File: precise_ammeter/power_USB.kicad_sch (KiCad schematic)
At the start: 0 parts

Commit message: Dodano Sekcje zasilanie MCU i wzmacniaczy oraz konektor USB
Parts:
- added C1, C22, C23, C25, C26, C5: 2u2, Capacitor_SMD:C_0805_2012Metric_Pad1.18x1.45mm_HandSolder, symbol Device:C
- added C24, C27: 10u, Capacitor_SMD:CP_Elec_4x5.4, symbol Device:C_Polarized
- added C28: 1n, Capacitor_SMD:C_0805_2012Metric_Pad1.18x1.45mm_HandSolder, symbol Device:C_Small
- added D1, D2: Green, LED_SMD:LED_0805_2012Metric_Pad1.15x1.40mm_HandSolder, symbol Device:LED
- added J3: USB4110GFA, USB4100GFA:GCT_USB4110GFA, symbol USB4110GFA:USB4110GFA
- added U10, U8: TPS7A2450DBVR, TPS7A2450DBVR:SOT_50DBVR, symbol TPS7A2450DBVR:TPS7A2450DBVR
- added U7: TPS7A2433DBVR, SOT23_DBV_TEX, symbol TPS7A2433DBVR:TPS7A2433DBVR
- added U9: LMC7660, Package_SO:SOIC-8_3.9x4.9mm_P1.27mm, symbol Regulator_SwitchedCapacitor:LMC7660
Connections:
- new net: C28.2, U9.7 (OSC)
- new net: C24.1, U9.2 (CAP+)
- new net: C24.2, U9.4 (CAP-)
- new net +3V3: C5.1, D2.2 (A), U7.5 (Vout)
- new net +5VA: C23.1, D1.2 (A), U8.5 (Vout)
- new net +5V_U9: C26.1, C28.1, U10.5 (Vout), U9.8 (V+)
- new net -5VA: C27.2, U9.5 (VOUT)
- new net GND: C1.2, C22.2, C23.2, C25.2, C26.2, C27.1, C5.2, D1.1 (K), D2.1 (K), J3.A1/B12 (GND), J3.B1/A12 (GND), J3.S1 (GND), J3.S2 (GND), J3.S3 (GND), J3.S4 (GND), U10.2 (GND), U7.2 (GND), U8.2 (GND), U9.3 (GND)
- new net USB_D_N: J3.A7 (DN1), J3.B7 (DN2)
- new net USB_D_P: J3.A6 (DP1), J3.B6 (DP2)
- new net VBUS: C1.1, C22.1, C25.1, U10.1 (Vin), U10.3 (EN), U7.1 (Vin), U7.3 (EN), U8.1 (Vin), U8.3 (EN)
- no-connect marks 0 -> 10
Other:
- note added: "+3V3 STM32 power supply"
- note added: "+5VA for analog section"
- note added: "-5VA for analog section"
- note added: "Power status LEDs"
- note added: "USB 2.0 Type C for data transfer only"

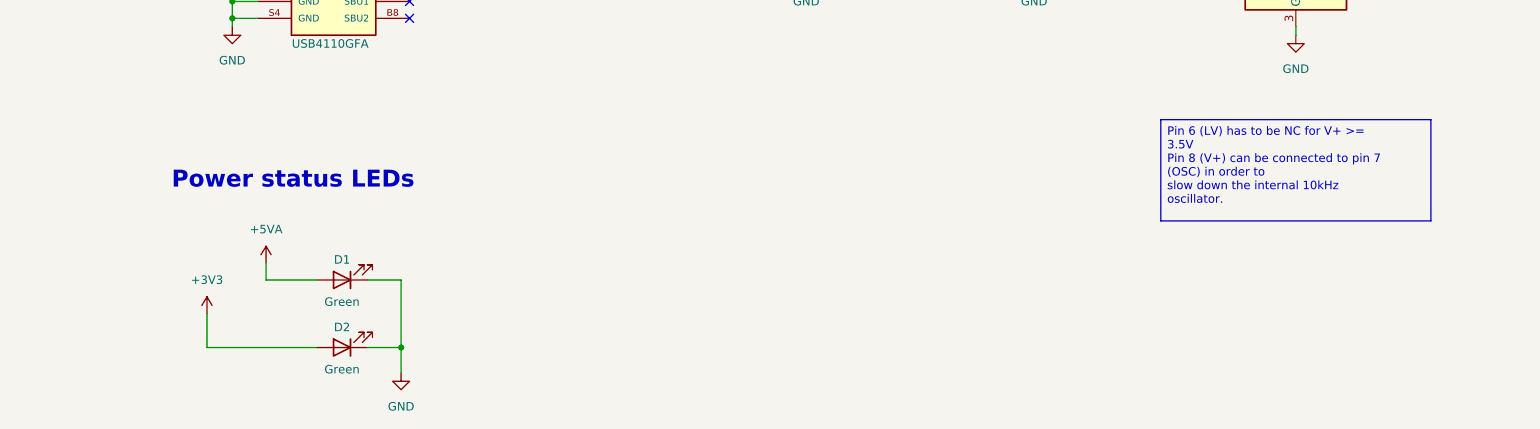
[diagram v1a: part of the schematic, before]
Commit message: dodano rezystory do diod LED
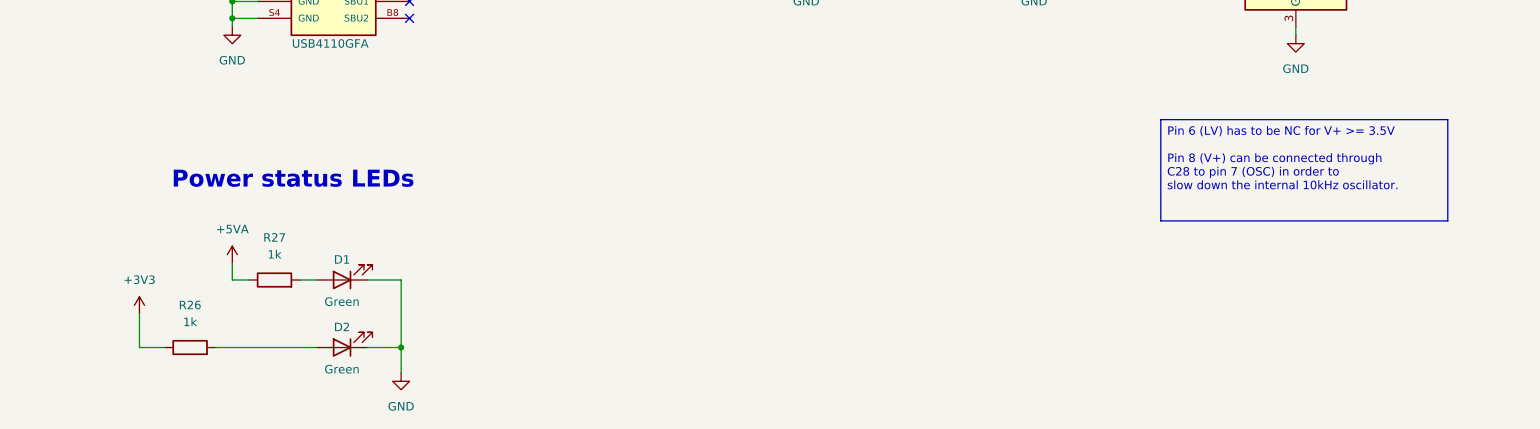
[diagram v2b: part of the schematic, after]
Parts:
- added R26, R27: 1k, Resistor_SMD:R_0805_2012Metric_Pad1.20x1.40mm_HandSolder, symbol Device:R
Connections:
- net +3V3: now also R26.1; no longer D2.2 (A)
- net +5VA: now also R27.1; no longer D1.2 (A)
- new net: D1.2 (A), R27.2
- new net: D2.2 (A), R26.2
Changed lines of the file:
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@@
 		)
 	)
-	(text_box "Pin 6 (LV) has to be NC for V+ >= 3.5V\nPin 8 (V+) can be connected to pin 7 (OSC) in order to\nslow down the internal 10kHz oscillator."
+	(text_box "Pin 6 (LV) has to be NC for V+ >= 3.5V\n\nPin 8 (V+) can be connected through C28 to pin 7 (OSC) in order to\nslow down the internal 10kHz oscillator."
 		(exclude_from_sim no)
 		(at 220.98 144.78 0)
-		(size 40.64 15.24)
+		(size 43.18 15.24)
 		(margins 0.9525 0.9525 0.9525 0.9525)
 		(stroke
@@
 	(wire
 		(pts
+			(xy 81.28 168.91) (xy 83.82 168.91)
+		)
+		(stroke
+			(width 0)
+			(type default)
+		)
+	)
+	(wire
+		(pts
 			(xy 198.12 45.72) (xy 198.12 44.45)
 		)
@@
 	(wire
 		(pts
-			(xy 93.98 179.07) (xy 77.47 179.07)
+			(xy 81.28 114.3) (xy 81.28 116.84)
 		)
 		(stroke
@@
 	(wire
 		(pts
-			(xy 81.28 114.3) (xy 81.28 116.84)
+			(xy 106.68 57.15) (xy 106.68 55.88)
 		)
 		(stroke
@@
 	(wire
 		(pts
-			(xy 106.68 57.15) (xy 106.68 55.88)
+			(xy 232.41 55.88) (xy 232.41 54.61)
 		)
 		(stroke
@@
 	(wire
 		(pts
-			(xy 232.41 55.88) (xy 232.41 54.61)
+			(xy 110.49 121.92) (xy 118.11 121.92)
 		)
 		(stroke
@@
 	(wire
 		(pts
-			(xy 110.49 121.92) (xy 118.11 121.92)
+			(xy 67.31 179.07) (xy 71.12 179.07)
 		)
 		(stroke
@@
 	(wire
 		(pts
+			(xy 78.74 179.07) (xy 93.98 179.07)
+		)
+		(stroke
+			(width 0)
+			(type default)
+		)
+	)
+	(wire
+		(pts
 			(xy 81.28 116.84) (xy 85.09 116.84)
 		)
@@
 	(wire
 		(pts
-			(xy 86.36 166.37) (xy 86.36 168.91)
+			(xy 81.28 166.37) (xy 81.28 168.91)
 		)
 		(stroke
@@
 	(wire
 		(pts
-			(xy 77.47 179.07) (xy 77.47 173.99)
+			(xy 67.31 179.07) (xy 67.31 173.99)
 		)
 		(stroke
@@
 	(wire
 		(pts
-			(xy 93.98 168.91) (xy 86.36 168.91)
-		)
-		(stroke
-			(width 0)
-			(type default)
-		)
-	)
-	(wire
-		(pts
 			(xy 81.28 124.46) (xy 85.09 124.46)
 		)
@@
 	(wire
 		(pts
+			(xy 91.44 168.91) (xy 93.98 168.91)
+		)
+		(stroke
+			(width 0)
+			(type default)
+		)
+	)
+	(wire
+		(pts
 			(xy 273.05 106.68) (xy 273.05 110.49)
 		)
@@
 	)
 	(symbol
+		(lib_id "Device:R")
+		(at 87.63 168.91 90)
+		(unit 1)
+		(exclude_from_sim no)
+		(in_bom yes)
+		(on_board yes)
+		(dnp no)
+		(fields_autoplaced yes)
+		(property "Reference" "R27"
+			(at 87.63 162.56 90)
+			(effects
+				(font
+					(size 1.27 1.27)
+				)
+			)
+		)
+		(property "Value" "1k"
+			(at 87.63 165.1 90)
+			(effects
+				(font
+					(size 1.27 1.27)
+				)
+			)
+		)
+		(property "Footprint" "Resistor_SMD:R_0805_2012Metric_Pad1.20x1.40mm_HandSolder"
+			(at 87.63 170.688 90)
+			(effects
+				(font
+					(size 1.27 1.27)
+				)
+				(hide yes)
+			)
+		)
+		(property "Datasheet" "~"
+			(at 87.63 168.91 0)
+			(effects
+				(font
+					(size 1.27 1.27)
+				)
+				(hide yes)
+			)
+		)
+		(property "Description" "Resistor"
+			(at 87.63 168.91 0)
+			(effects
+				(font
+					(size 1.27 1.27)
+				)
+				(hide yes)
+			)
+		)
+		(pin "2"
+		)
+		(pin "1"
+		)
+		(instances
+			(project ""
+				(path "/7da3b652-85ac-4caa-8d8d-9cad461e9c85/9e6d6147-95e6-4ef0-a238-5628802dd2a2"
+					(reference "R27")
+					(unit 1)
+				)
+			)
+		)
+	)
+	(symbol
 		(lib_id "Device:C_Small")
 		(at 224.79 114.3 0)
@@
 	(symbol
 		(lib_id "power:+5VA")
-		(at 86.36 166.37 0)
+		(at 81.28 166.37 0)
 		(unit 1)
 		(exclude_from_sim no)
@@
 		(fields_autoplaced yes)
 		(property "Reference" "#PWR062"
-			(at 86.36 170.18 0)
+			(at 81.28 170.18 0)
 			(effects
 				(font
@@
 		)
 		(property "Value" "+5VA"
-			(at 86.36 161.29 0)
+			(at 81.28 161.29 0)
 			(effects
 				(font
@@
 		)
 		(property "Footprint" ""
-			(at 86.36 166.37 0)
+			(at 81.28 166.37 0)
 			(effects
 				(font
@@
 		)
 		(property "Datasheet" ""
-			(at 86.36 166.37 0)
+			(at 81.28 166.37 0)
 			(effects
 				(font
@@
 		)
 		(property "Description" "Power symbol creates a global label with name \"+5VA\""
-			(at 86.36 166.37 0)
+			(at 81.28 166.37 0)
 			(effects
 				(font
@@
 	)
 	(symbol
+		(lib_id "Device:R")
+		(at 74.93 179.07 90)
+		(unit 1)
+		(exclude_from_sim no)
+		(in_bom yes)
+		(on_board yes)
+		(dnp no)
+		(fields_autoplaced yes)
+		(property "Reference" "R26"
+			(at 74.93 172.72 90)
+			(effects
+				(font
+					(size 1.27 1.27)
+				)
+			)
+		)
+		(property "Value" "1k"
+			(at 74.93 175.26 90)
+			(effects
+				(font
+					(size 1.27 1.27)
+				)
+			)
+		)
+		(property "Footprint" "Resistor_SMD:R_0805_2012Metric_Pad1.20x1.40mm_HandSolder"
+			(at 74.93 180.848 90)
+			(effects
+				(font
+					(size 1.27 1.27)
+				)
+				(hide yes)
+			)
+		)
+		(property "Datasheet" "~"
+			(at 74.93 179.07 0)
+			(effects
+				(font
+					(size 1.27 1.27)
+				)
+				(hide yes)
+			)
+		)
+		(property "Description" "Resistor"
+			(at 74.93 179.07 0)
+			(effects
+				(font
+					(size 1.27 1.27)
+				)
+				(hide yes)
+			)
+		)
+		(pin "2"
+		)
+		(pin "1"
+		)
+		(instances
+			(project ""
+				(path "/7da3b652-85ac-4caa-8d8d-9cad461e9c85/9e6d6147-95e6-4ef0-a238-5628802dd2a2"
+					(reference "R26")
+					(unit 1)
+				)
+			)
+		)
+	)
+	(symbol
 		(lib_id "power:GND")
 		(at 72.39 57.15 0)
@@
 	(symbol
 		(lib_id "power:+3V3")
-		(at 77.47 173.99 0)
+		(at 67.31 173.99 0)
 		(unit 1)
 		(exclude_from_sim no)
@@
 		(fields_autoplaced yes)
 		(property "Reference" "#PWR063"
-			(at 77.47 177.8 0)
+			(at 67.31 177.8 0)
 			(effects
 				(font
@@
 		)
 		(property "Value" "+3V3"
-			(at 77.47 168.91 0)
+			(at 67.31 168.91 0)
 			(effects
 				(font
@@
 		)
 		(property "Footprint" ""
-			(at 77.47 173.99 0)
+			(at 67.31 173.99 0)
 			(effects
 				(font
@@
 		)
 		(property "Datasheet" ""
-			(at 77.47 173.99 0)
+			(at 67.31 173.99 0)
 			(effects
 				(font
@@
 		)
 		(property "Description" "Power symbol creates a global label with name \"+3V3\""
-			(at 77.47 173.99 0)
+			(at 67.31 173.99 0)
 			(effects
 				(font

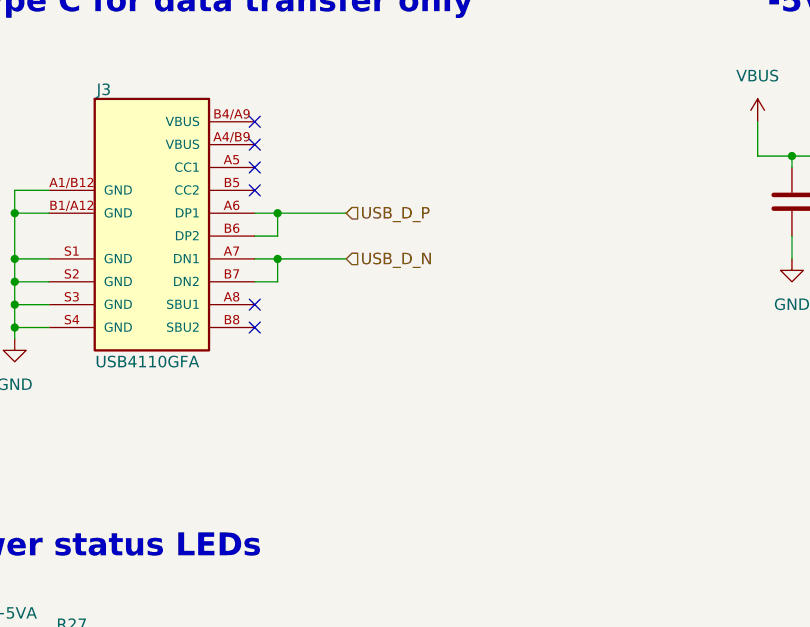
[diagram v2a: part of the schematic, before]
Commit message: Dodane pull down na piny CC USB
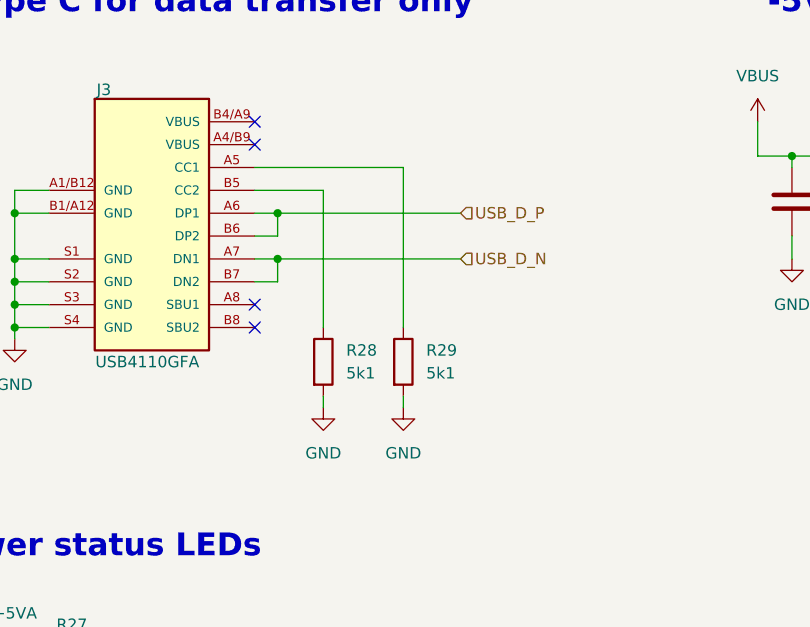
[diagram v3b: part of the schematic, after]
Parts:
- added R28, R29: 5k1, Resistor_SMD:R_0805_2012Metric_Pad1.20x1.40mm_HandSolder, symbol Device:R
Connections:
- net GND: now also R28.2, R29.2
- net at J3.A5 (CC1): now also R29.1
- net at J3.B5 (CC2): now also R28.1
- no-connect marks 10 -> 8

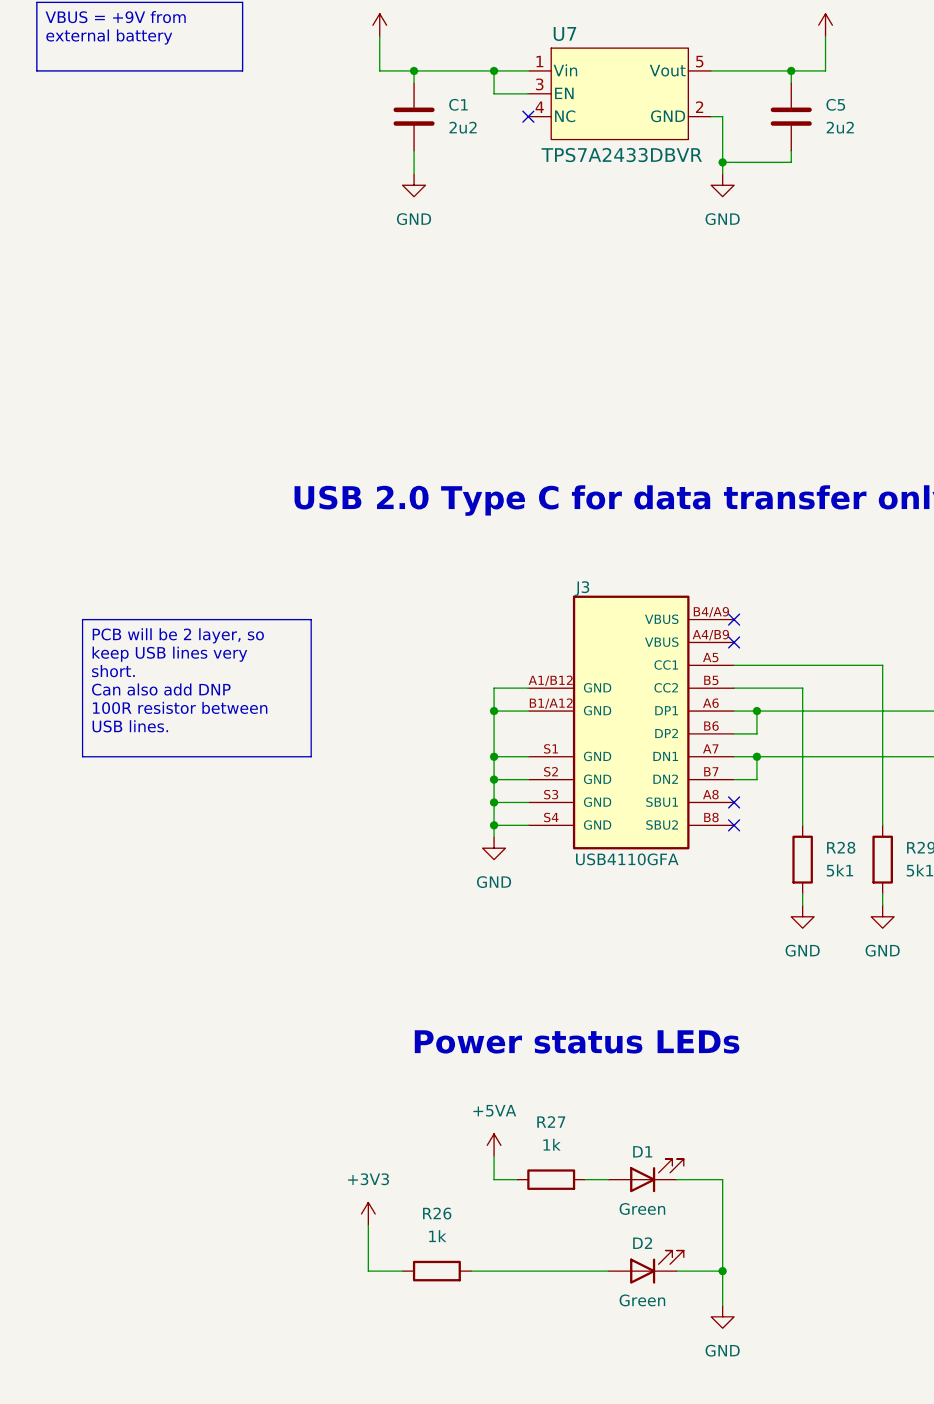
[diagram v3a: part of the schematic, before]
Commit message: Dodano konektor XT30 dla baterii i zrobiono adnotacj diod Schotkiego na schemacie MCU
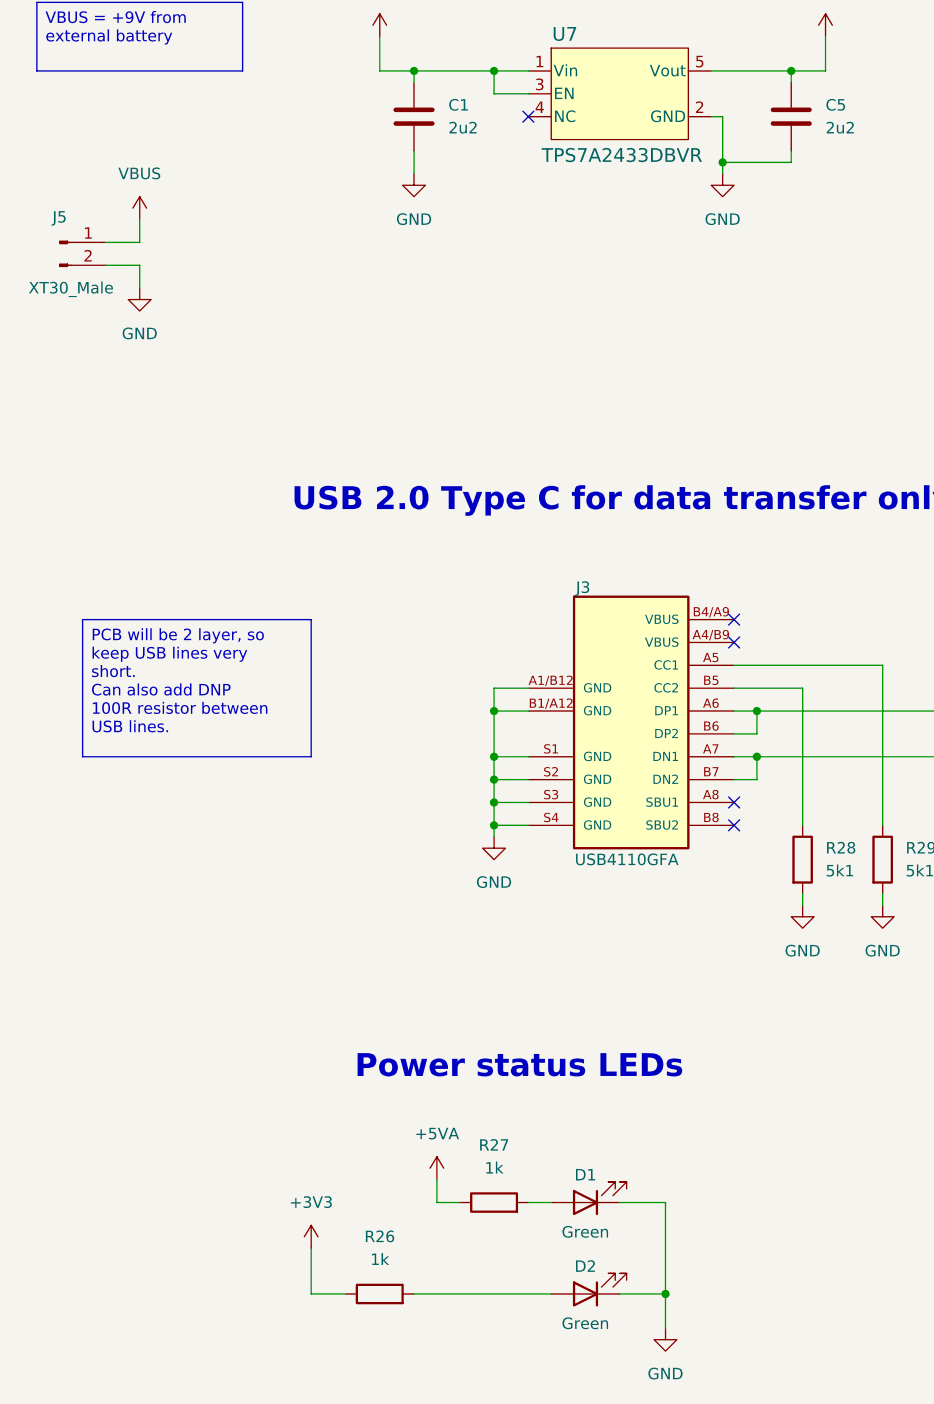
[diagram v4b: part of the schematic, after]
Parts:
- added J5: XT30_Male, Connector_AMASS:AMASS_XT30UPB-M_1x02_P5.0mm_Vertical, symbol Connector:Conn_01x02_Pin
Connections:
- net GND: now also J5.2 (Pin_2)
- net VBUS: now also J5.1 (Pin_1)
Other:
- moved on the sheet: D1, D2, R26, R27
